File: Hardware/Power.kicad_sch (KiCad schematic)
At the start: 14 parts, among them J1 Conn_01x02_Pin, SW2 SW_SPST, U1 TPS5430DDA

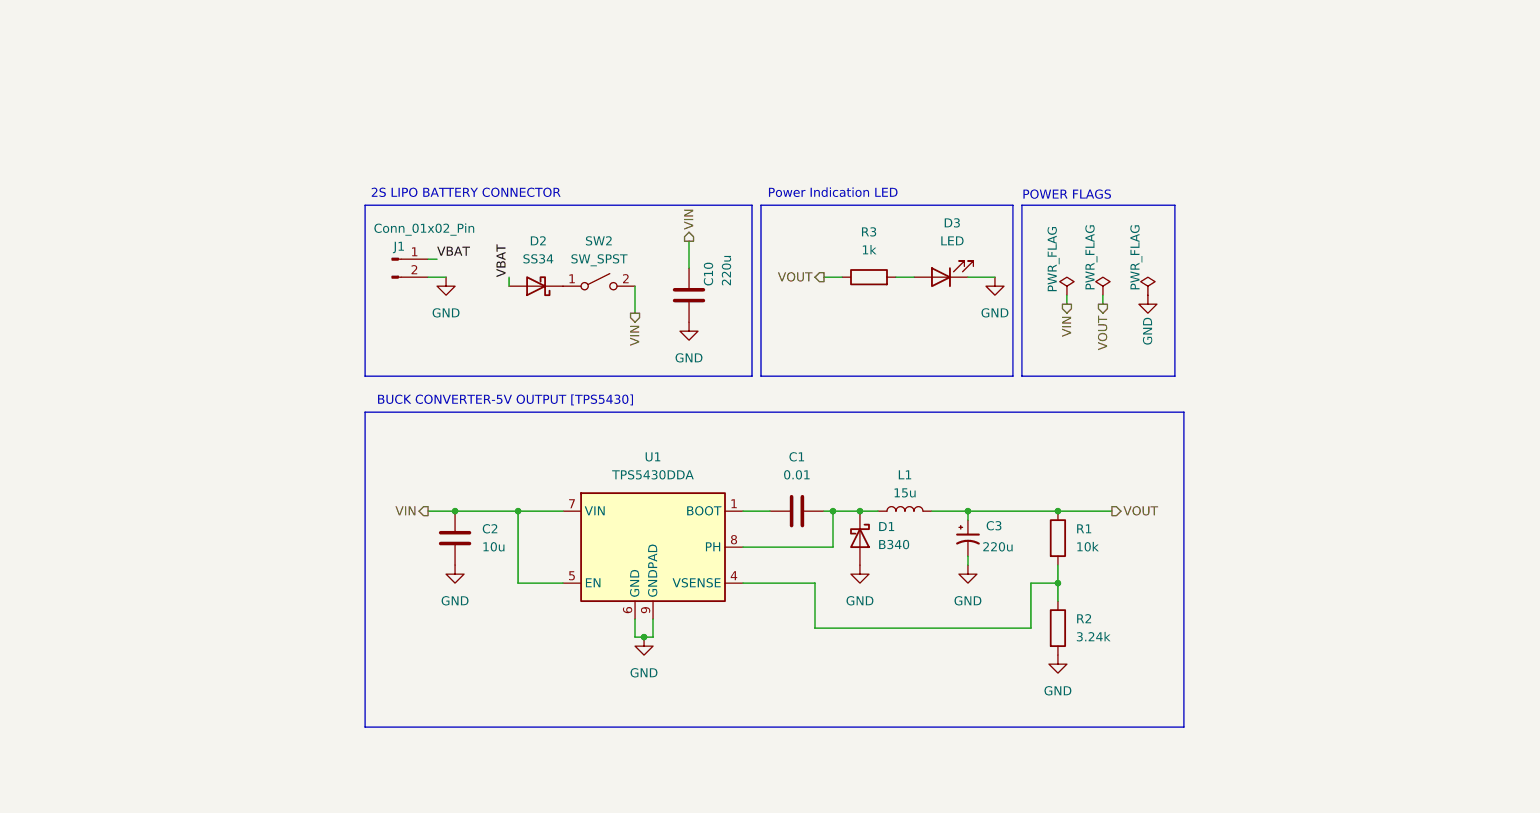
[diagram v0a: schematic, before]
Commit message: Schematic updated with buck and motor driver breakout boards
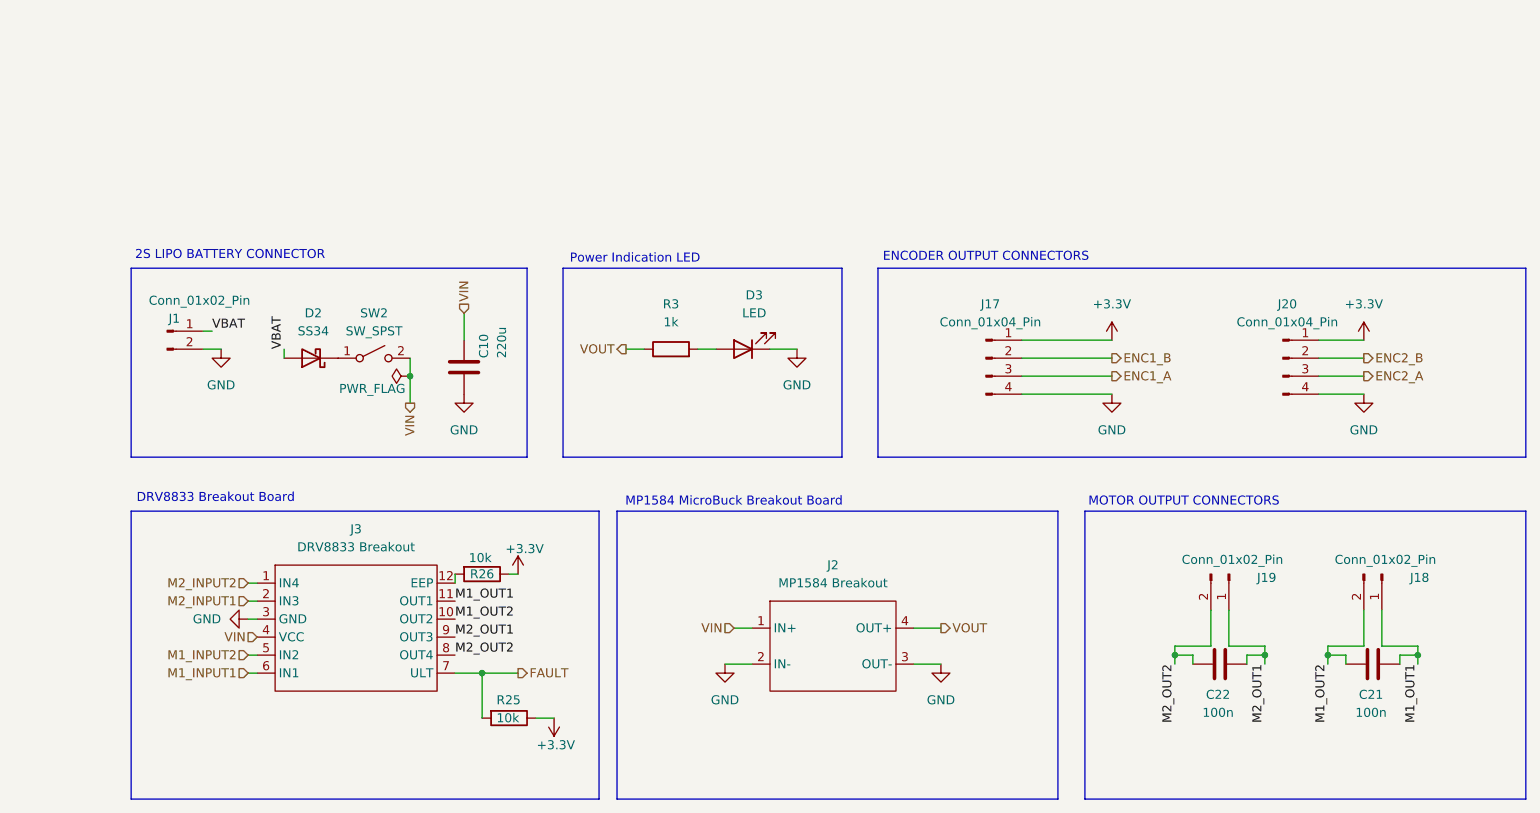
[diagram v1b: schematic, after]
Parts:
- removed C1: 0.01, symbol Device:C
- removed C2: 10u, symbol Device:C
- removed C3: 220u, symbol Device:C_Polarized_Small_US
- removed D1: B340, Diode_SMD:D_SMC, symbol Diode:B340
- removed L1: 15u, symbol Device:L
- removed R1: 10k, symbol Device:R
- removed R2: 3.24k, symbol Device:R
- removed U1: TPS5430DDA, Package_SO:TI_SO-PowerPAD-8_ThermalVias, symbol Regulator_Switching:TPS5430DDA
- added C21, C22: 100n, symbol Device:C
- added J17, J20: Conn_01x04_Pin, symbol Connector:Conn_01x04_Pin
- added J18, J19: Conn_01x02_Pin, symbol Connector:Conn_01x02_Pin
- added J2: MP1584 Breakout, symbol HSM_Symbols:MP1584_MicroBuck
- added J3: DRV8833 Breakout, symbol HSM_Symbols:DRV8833_Breakout
- added R25, R26: 10k, symbol Device:R
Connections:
- net GND: now also J17.4 (Pin_4), J2.2 (IN-), J2.3 (OUT-), J20.4 (Pin_4), J3.3 (GND)
- net VIN: now also J2.1 (IN+), J3.4 (VCC)
- net VOUT: now also J2.4 (OUT+)
- new net: J3.12 (EEP), R26.2
- new net +3.3V: J17.1 (Pin_1), J20.1 (Pin_1), R25.1, R26.1
- new net ENC1_A: J17.3 (Pin_3)
- new net ENC1_B: J17.2 (Pin_2)
- new net ENC2_A: J20.3 (Pin_3)
- new net ENC2_B: J20.2 (Pin_2)
- new net FAULT: J3.7 (ULT), R25.2
- new net M1_INPUT1: J3.6 (IN1)
- new net M1_INPUT2: J3.5 (IN2)
- new net M1_OUT1: C21.2, J18.1 (Pin_1), J3.11 (OUT1)
- new net M1_OUT2: C21.1, J18.2 (Pin_2), J3.10 (OUT2)
- new net M2_INPUT1: J3.2 (IN3)
- new net M2_INPUT2: J3.1 (IN4)
- new net M2_OUT1: C22.2, J19.1 (Pin_1), J3.9 (OUT3)
- new net M2_OUT2: C22.1, J19.2 (Pin_2), J3.8 (OUT4)
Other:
- note added: "DRV8833 Breakout Board"
- note added: "ENCODER OUTPUT CONNECTORS"
- note added: "MOTOR OUTPUT CONNECTORS"
- note added: "MP1584 MicroBuck Breakout Board"
- note removed: "BUCK CONVERTER-5V OUTPUT [TPS5430]"
- note removed: "POWER FLAGS"
- moved on the sheet: C10, D2, D3, J1, R3, SW2

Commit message: Switches changed,added low pass filters, emitter caps
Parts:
- removed SW2: SW_SPST, symbol Switch:SW_SPST
- added SW2: SW_SPDT, symbol Switch:SW_SPDT
- C10, C21, C22: footprint (none) -> Capacitor_SMD:C_0603_1608Metric
- D3: footprint (none) -> LED_SMD:LED_0603_1608Metric
- J1: footprint (none) -> Connector_JST:JST_XH_B2B-XH-A_1x02_P2.50mm_Vertical
- J17, J20: footprint (none) -> Connector_JST:JST_PH_B4B-PH-K_1x04_P2.00mm_Vertical
- J18, J19: footprint (none) -> Connector_JST:JST_PH_B2B-PH-K_1x02_P2.00mm_Vertical
- J2: footprint (none) -> Micromouse_Footprints:SRT_MPT1584EN_Module
- J3: footprint (none) -> Micromouse_Footprints:DRV8833
- R25, R26, R3: footprint (none) -> Resistor_SMD:R_0603_1608Metric
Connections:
- net GND: now also J2.4 (IN-), J2.5 (OUT-), J2.6 (OUT-); no longer J2.2 (IN-)
- net VOUT: now also J2.7 (OUT+), J2.8 (OUT+); no longer J2.4 (OUT+)
- net at D2.1 (K): now also SW2.2 (B)
- net VIN renamed IN+
- net IN+: now also J2.2 (IN+), SW2.3 (C)
- no-connect marks 0 -> 1

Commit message: Added KiCad PCB files
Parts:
- SW2: footprint (none) -> Button_Switch_SMD:SW_SPDT_CK_JS102011SAQN
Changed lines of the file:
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@@
 			)
 		)
-		(property "Footprint" ""
+		(property "Footprint" "Button_Switch_SMD:SW_SPDT_CK_JS102011SAQN"
 			(at 83.82 68.58 0)
 			(effects

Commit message: Added the mounting holes, kill iwtch for the moto,removed resistors from xshut, and some others
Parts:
- added H1, H2, H3, H4: MountingHole, MountingHole:MountingHole_2mm, symbol Mechanical:MountingHole
- added SW1: SW_SPDT, Button_Switch_SMD:SW_SPDT_CK_JS102011SAQN, symbol Switch:SW_SPDT
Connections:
- net IN+: now also SW1.2 (B); no longer J3.4 (VCC)
- new net: J3.4 (VCC), SW1.3 (C)
- no-connect marks 1 -> 2
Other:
- note added: "Mounting holes"

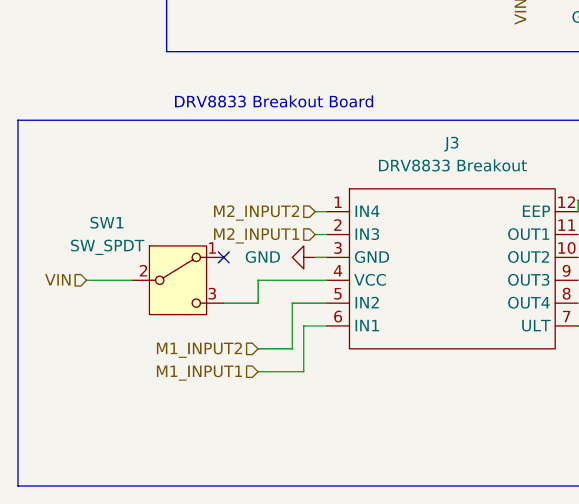
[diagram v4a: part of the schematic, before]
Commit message: 1)PCB tracing continued, power traces need to verified,signal traces almost done except xshut, need to verify drv8833 dimesnions, should resolve teensy 4.1 error, switches footprint need to be changed. 2) changed schematic for optimum tracing in pcb editor,removed oled and added one more extra i2c bus to prevent i2c locking
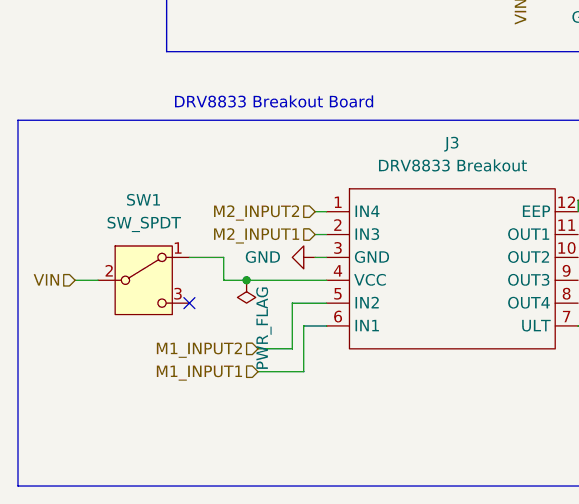
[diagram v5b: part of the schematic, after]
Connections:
- net at SW1.1 (A): now also J3.4 (VCC)
- net at SW1.3 (C): no longer J3.4 (VCC)
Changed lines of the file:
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@@
+	)
+	(junction
+		(at 58.42 113.03)
+		(diameter 0)
+		(color 0 0 0 0)
 	)
 	(junction
@@
 	)
 	(no_connect
-		(at 55.88 110.49)
+		(at 52.07 115.57)
 	)
 	(wire
@@
 	(wire
 		(pts
-			(xy 59.69 115.57) (xy 59.69 113.03)
-		)
-		(stroke
-			(width 0)
-			(type default)
-		)
-	)
-	(wire
-		(pts
 			(xy 218.44 115.57) (xy 218.44 116.84)
 		)
@@
 	(wire
 		(pts
-			(xy 40.64 113.03) (xy 45.72 113.03)
-		)
-		(stroke
-			(width 0)
-			(type default)
-		)
-	)
-	(wire
-		(pts
 			(xy 160.02 111.76) (xy 163.83 111.76)
 		)
@@
 	(wire
 		(pts
+			(xy 55.88 110.49) (xy 55.88 113.03)
+		)
+		(stroke
+			(width 0)
+			(type default)
+		)
+	)
+	(wire
+		(pts
 			(xy 59.69 72.39) (xy 62.23 72.39)
 		)
@@
 	(wire
 		(pts
+			(xy 58.42 113.03) (xy 67.31 113.03)
+		)
+		(stroke
+			(width 0)
+			(type default)
+		)
+	)
+	(wire
+		(pts
 			(xy 218.44 115.57) (xy 220.98 115.57)
 		)
@@
 	(wire
 		(pts
+			(xy 52.07 110.49) (xy 55.88 110.49)
+		)
+		(stroke
+			(width 0)
+			(type default)
+		)
+	)
+	(wire
+		(pts
 			(xy 223.52 114.3) (xy 223.52 109.22)
 		)
@@
 	(wire
 		(pts
+			(xy 39.37 113.03) (xy 41.91 113.03)
+		)
+		(stroke
+			(width 0)
+			(type default)
+		)
+	)
+	(wire
+		(pts
 			(xy 175.26 73.66) (xy 187.96 73.66)
 		)
@@
 	(wire
 		(pts
-			(xy 55.88 115.57) (xy 59.69 115.57)
-		)
-		(stroke
-			(width 0)
-			(type default)
-		)
-	)
-	(wire
-		(pts
 			(xy 119.38 72.39) (xy 121.92 72.39)
 		)
@@
 	(wire
 		(pts
+			(xy 55.88 113.03) (xy 58.42 113.03)
+		)
+		(stroke
+			(width 0)
+			(type default)
+		)
+	)
+	(wire
+		(pts
 			(xy 231.14 114.3) (xy 226.06 114.3)
 		)
@@
 		(pts
 			(xy 66.04 107.95) (xy 67.31 107.95)
-		)
-		(stroke
-			(width 0)
-			(type default)
-		)
-	)
-	(wire
-		(pts
-			(xy 59.69 113.03) (xy 67.31 113.03)
 		)
 		(stroke
@@
 	(hierarchical_label "VIN"
 		(shape input)
-		(at 40.64 113.03 180)
+		(at 39.37 113.03 180)
 		(effects
 			(font
@@
 	)
 	(symbol
-		(lib_id "Switch:SW_SPDT")
-		(at 50.8 113.03 0)
-		(unit 1)
-		(exclude_from_sim no)
-		(in_bom yes)
-		(on_board yes)
-		(dnp no)
-		(property "Reference" "SW1"
-			(at 42.926 106.68 0)
-			(effects
-				(font
-					(size 1.27 1.27)
-				)
-			)
-		)
-		(property "Value" "SW_SPDT"
-			(at 42.926 109.22 0)
-			(effects
-				(font
-					(size 1.27 1.27)
-				)
-			)
-		)
-		(property "Footprint" "Button_Switch_SMD:SW_SPDT_CK_JS102011SAQN"
-			(at 50.8 113.03 0)
-			(effects
-				(font
-					(size 1.27 1.27)
-				)
-				(hide yes)
-			)
-		)
-		(property "Datasheet" "~"
-			(at 50.8 120.65 0)
-			(effects
-				(font
-					(size 1.27 1.27)
-				)
-				(hide yes)
-			)
-		)
-		(property "Description" "Switch, single pole double throw"
-			(at 50.8 113.03 0)
-			(effects
-				(font
-					(size 1.27 1.27)
-				)
-				(hide yes)
-			)
-		)
-		(pin "2"
-		)
-		(pin "3"
-		)
-		(pin "1"
-		)
-		(instances
-			(project "HSM_Project"
-				(path "/10a490ba-03bd-419b-97f3-e1946b38fc40/ac18e862-6ffc-44ea-b67e-4cb824815cfe"
-					(reference "SW1")
-					(unit 1)
-				)
-			)
-		)
-	)
-	(symbol
 		(lib_id "power:GND")
 		(at 163.83 116.84 0)
@@
 	)
 	(symbol
+		(lib_id "Switch:SW_SPDT")
+		(at 46.99 113.03 0)
+		(unit 1)
+		(exclude_from_sim no)
+		(in_bom yes)
+		(on_board yes)
+		(dnp no)
+		(fields_autoplaced yes)
+		(property "Reference" "SW1"
+			(at 46.99 104.14 0)
+			(effects
+				(font
+					(size 1.27 1.27)
+				)
+			)
+		)
+		(property "Value" "SW_SPDT"
+			(at 46.99 106.68 0)
+			(effects
+				(font
+					(size 1.27 1.27)
+				)
+			)
+		)
+		(property "Footprint" "Button_Switch_SMD:SW_SPDT_CK_JS102011SAQN"
+			(at 46.99 113.03 0)
+			(effects
+				(font
+					(size 1.27 1.27)
+				)
+				(hide yes)
+			)
+		)
+		(property "Datasheet" "~"
+			(at 46.99 120.65 0)
+			(effects
+				(font
+					(size 1.27 1.27)
+				)
+				(hide yes)
+			)
+		)
+		(property "Description" "Switch, single pole double throw"
+			(at 46.99 113.03 0)
+			(effects
+				(font
+					(size 1.27 1.27)
+				)
+				(hide yes)
+			)
+		)
+		(pin "2"
+		)
+		(pin "1"
+		)
+		(pin "3"
+		)
+		(instances
+			(project ""
+				(path "/10a490ba-03bd-419b-97f3-e1946b38fc40/ac18e862-6ffc-44ea-b67e-4cb824815cfe"
+					(reference "SW1")
+					(unit 1)
+				)
+			)
+		)
+	)
+	(symbol
 		(lib_id "HSM_Symbols:DRV8833_Breakout")
 		(at 81.28 110.49 0)
@@
 					(unit 1)
 				)
+			)
+		)
+	)
+	(symbol
+		(lib_id "power:PWR_FLAG")
+		(at 58.42 113.03 180)
+		(unit 1)
+		(exclude_from_sim no)
+		(in_bom yes)
+		(on_board yes)
+		(dnp no)
+		(property "Reference" "#FLG01"
+			(at 58.42 114.935 0)
+			(effects
+				(font
+					(size 1.27 1.27)
+				)
+				(hide yes)
+			)
+		)
+		(property "Value" "PWR_FLAG"
+			(at 60.198 118.364 90)
+			(effects
+				(font
+					(size 1.27 1.27)
+				)
+			)
+		)
+		(property "Footprint" ""
+			(at 58.42 113.03 0)
+			(effects
+				(font
+					(size 1.27 1.27)
+				)
+				(hide yes)
+			)
+		)
+		(property "Datasheet" "~"
+			(at 58.42 113.03 0)
+			(effects
+				(font
+					(size 1.27 1.27)
+				)
+				(hide yes)
+			)
+		)
+		(property "Description" "Special symbol for telling ERC where power comes from"
+			(at 58.42 113.03 0)
+			(effects
+				(font
+					(size 1.27 1.27)
+				)
+				(hide yes)
+			)
+		)
+		(pin "1"
+		)
+		(instances
+			(project "HSM_Project"
+				(path "/10a490ba-03bd-419b-97f3-e1946b38fc40/ac18e862-6ffc-44ea-b67e-4cb824815cfe"
+					(reference "#FLG01")
+					(unit 1)
+				)

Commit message: Final updated pcb and schematic before dfm check
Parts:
- removed J17, J20: Conn_01x04_Pin, Connector_JST:JST_PH_B4B-PH-K_1x04_P2.00mm_Vertical, symbol Connector:Conn_01x04_Pin
- removed J18, J19: Conn_01x02_Pin, Connector_JST:JST_PH_B2B-PH-K_1x02_P2.00mm_Vertical, symbol Connector:Conn_01x02_Pin
- added F1: Fuse, Fuse:Fuse_1206_3216Metric_Pad1.42x1.75mm_HandSolder, symbol Device:Fuse
- added H10, H5, H6, H7, H8, H9: MountingHole, MountingHole:MountingHole_2mm, symbol Mechanical:MountingHole
- added J6, J7: Conn_01x06_Pin, Connector_PinHeader_2.54mm:PinHeader_1x06_P2.54mm_Vertical, symbol Connector:Conn_01x06_Pin
- C10, C21, C22: footprint Capacitor_SMD:C_0603_1608Metric -> Capacitor_SMD:C_0603_1608Metric_Pad1.08x0.95mm_HandSolder
- D2: footprint Diode_SMD:D_SMA -> Diode_SMD:D_SMA_Handsoldering
- D3: footprint LED_SMD:LED_0603_1608Metric -> LED_THT:LED_D3.0mm
- J1: footprint Connector_JST:JST_XH_B2B-XH-A_1x02_P2.50mm_Vertical -> Connector_AMASS:AMASS_XT60-M_1x02_P7.20mm_Vertical
- R25, R26, R3: footprint Resistor_SMD:R_0603_1608Metric -> Resistor_SMD:R_0603_1608Metric_Pad0.98x0.95mm_HandSolder
- SW1, SW2: footprint Button_Switch_SMD:SW_SPDT_CK_JS102011SAQN -> Button_Switch_THT:SW_Slide_SPDT_Angled_CK_OS102011MA1Q
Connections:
- net +3.3V: now also J6.5 (Pin_5), J7.5 (Pin_5)
- net ENC1_A: now also J6.3 (Pin_3)
- net ENC1_B: now also J6.4 (Pin_4)
- net ENC2_A: now also J7.3 (Pin_3)
- net ENC2_B: now also J7.4 (Pin_4)
- net GND: now also J6.2 (Pin_2), J7.2 (Pin_2)
- net IN+: no longer C10.1
- net M1_OUT1: now also J6.1 (Pin_1)
- net M1_OUT2: now also J6.6 (Pin_6)
- net M2_OUT1: now also J7.1 (Pin_1)
- net M2_OUT2: now also J7.6 (Pin_6)
- net at D2.1 (K), SW2.2 (B): now also C10.1
- net VBAT: no longer names the net of D2.2 (A)
- net VBAT: now also F1.2; no longer J1.1 (Pin_1)
- net VOUT renamed +5V
- new net: F1.1, J1.1 (Pin_1)
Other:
- note added: "MOTOR AND ENCODER OUTPUT CONNECTORS"
- note removed: "ENCODER OUTPUT CONNECTORS"
- note removed: "MOTOR OUTPUT CONNECTORS"
- moved on the sheet: C10, C21, C22, D2, D3, H1, H2, H3, H4, J1, J2, J3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

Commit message: Ignore KiCad .history folder
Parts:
- H1, H10, H2, H3, H4, H5, H6, H7, H8, H9: footprint MountingHole:MountingHole_2mm -> MountingHole:MountingHole_2.1mm
- J2: footprint Micromouse_Footprints:SRT_MPT1584EN_Module -> Micromouse:MP1584
- J3: footprint Micromouse_Footprints:DRV8833 -> Micromouse:DRV8833

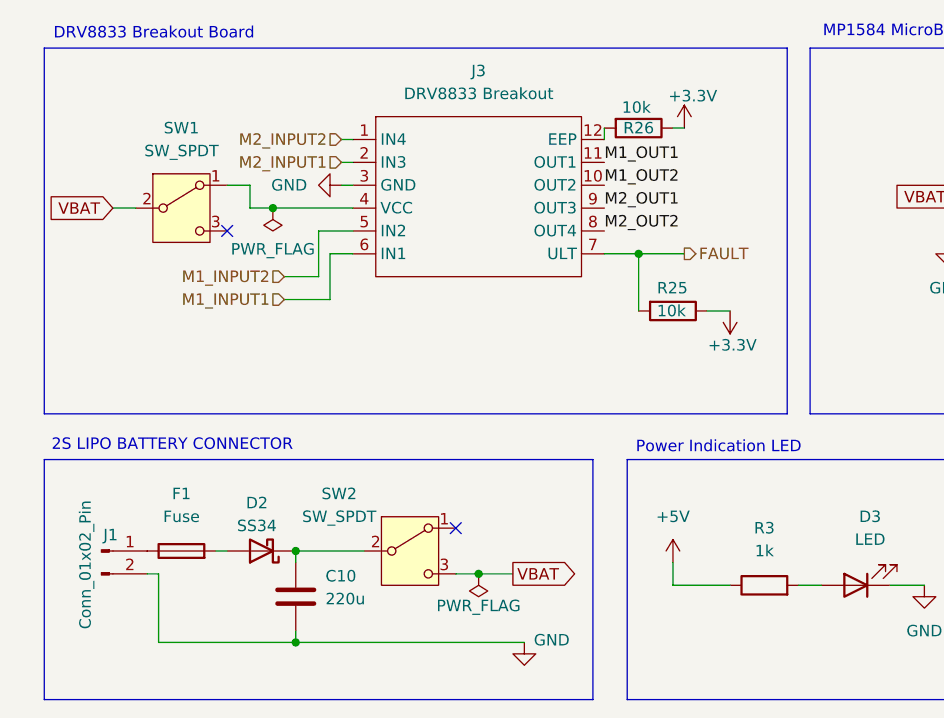
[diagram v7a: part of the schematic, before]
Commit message: updated the dimensiosn of tb6612,shifted placements based on dfm check, other changes
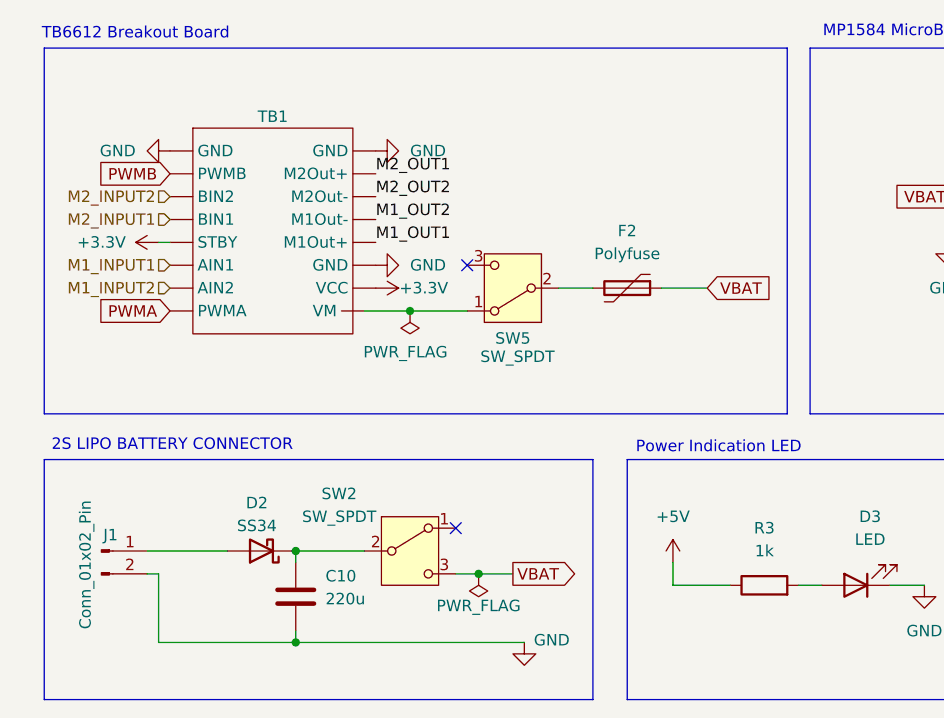
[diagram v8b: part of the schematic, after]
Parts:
- removed F1: Fuse, Fuse:Fuse_1206_3216Metric_Pad1.42x1.75mm_HandSolder, symbol Device:Fuse
- removed J3: DRV8833 Breakout, Micromouse:DRV8833, symbol HSM_Symbols:DRV8833_Breakout
- removed R25, R26: 10k, Resistor_SMD:R_0603_1608Metric_Pad0.98x0.95mm_HandSolder, symbol Device:R
- removed SW1: SW_SPDT, Button_Switch_THT:SW_Slide_SPDT_Angled_CK_OS102011MA1Q, symbol Switch:SW_SPDT
- added F2: Polyfuse, Fuse:Fuse_Bourns_MF-SM_9.5x6.71mm, symbol Device:Polyfuse
- added SW5: SW_SPDT, Button_Switch_THT:SW_Slide_SPDT_Angled_CK_OS102011MA1Q, symbol Switch:SW_SPDT
- added TB1: (no value), TB6612:TB6612 module, symbol tb6612_module:TB6612_module
- C10: footprint Capacitor_SMD:C_0603_1608Metric_Pad1.08x0.95mm_HandSolder -> Capacitor_THT:CP_Radial_D6.3mm_P2.50mm
- J1: footprint Connector_AMASS:AMASS_XT60-M_1x02_P7.20mm_Vertical -> Connector_AMASS:AMASS_XT30UPB-M_1x02_P5.0mm_Vertical
- J6, J7: footprint Connector_PinHeader_2.54mm:PinHeader_1x06_P2.54mm_Vertical -> Connector_JST:JST_PH_B6B-PH-K_1x06_P2.00mm_Vertical
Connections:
- net +3.3V: now also TB1.15 (VCC), TB1.5 (STBY)
- net GND: now also TB1.1 (GND), TB1.14 (GND), TB1.9 (GND)
- net IN+: now also F2.1
- net M1_INPUT1: now also TB1.6 (AIN1)
- net M1_INPUT2: now also TB1.7 (AIN2)
- net M1_OUT1: now also TB1.13 (M1Out+)
- net M1_OUT2: now also TB1.12 (M1Out-)
- net M2_INPUT1: now also TB1.4 (BIN1)
- net M2_INPUT2: now also TB1.3 (BIN2)
- net M2_OUT1: now also TB1.10 (M2Out+)
- net M2_OUT2: now also TB1.11 (M2Out-)
- net at D2.2 (A): now also J1.1 (Pin_1)
- new net: SW5.1 (A), TB1.16 (VM)
- new net: F2.2, SW5.2 (B)
- new net PWMA: TB1.8 (PWMA)
- new net PWMB: TB1.2 (PWMB)
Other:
- note added: "TB6612 Breakout Board"
- note removed: "DRV8833 Breakout Board"
